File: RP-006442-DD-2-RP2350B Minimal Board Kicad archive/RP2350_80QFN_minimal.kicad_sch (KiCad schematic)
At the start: 51 parts, among them J1 USB_C_Receptacle_USB2.0_16P, J2 Conn_02x26_Odd_Even, J3 Conn_02x26_Odd_Even, J4 SM03B-SRSS-TB, SW1 SW_Push, SW2 SW_Push, U1 RP2350_80QFN, U2 NCP1117-3.3_SOT223, U3 W25Q128JVS, U4 DNF, Y1 ABM8-272-T3

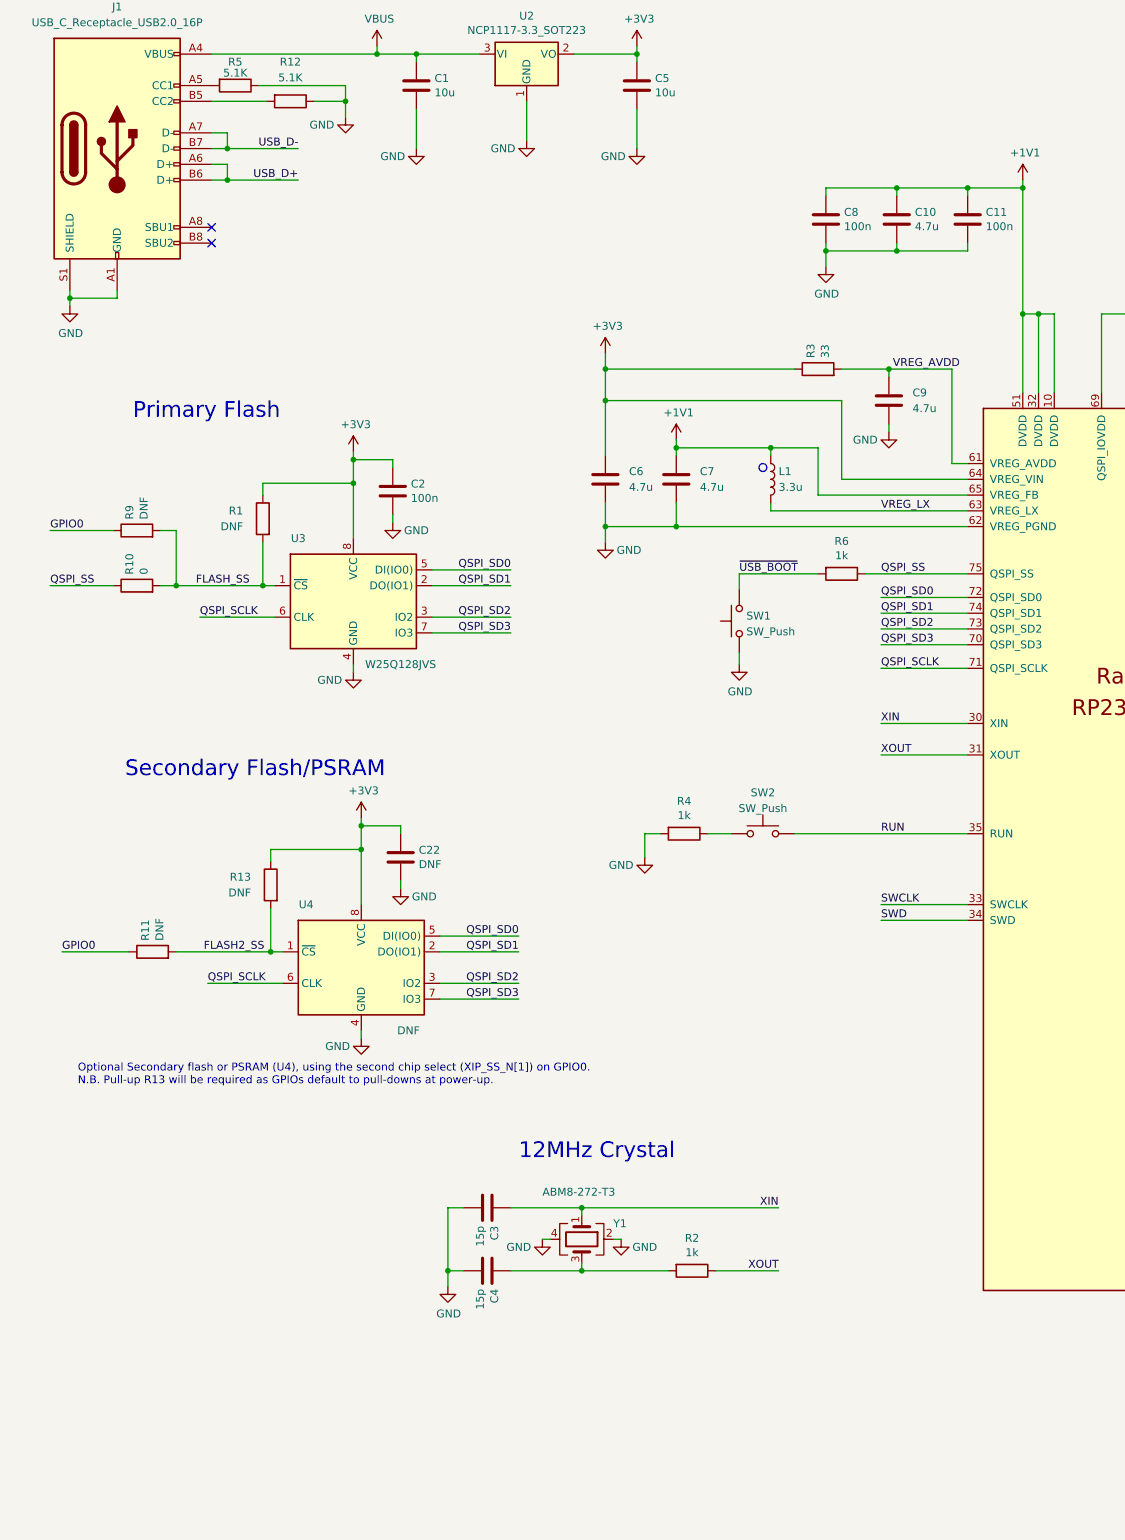
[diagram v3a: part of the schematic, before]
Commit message: added leds schematic page
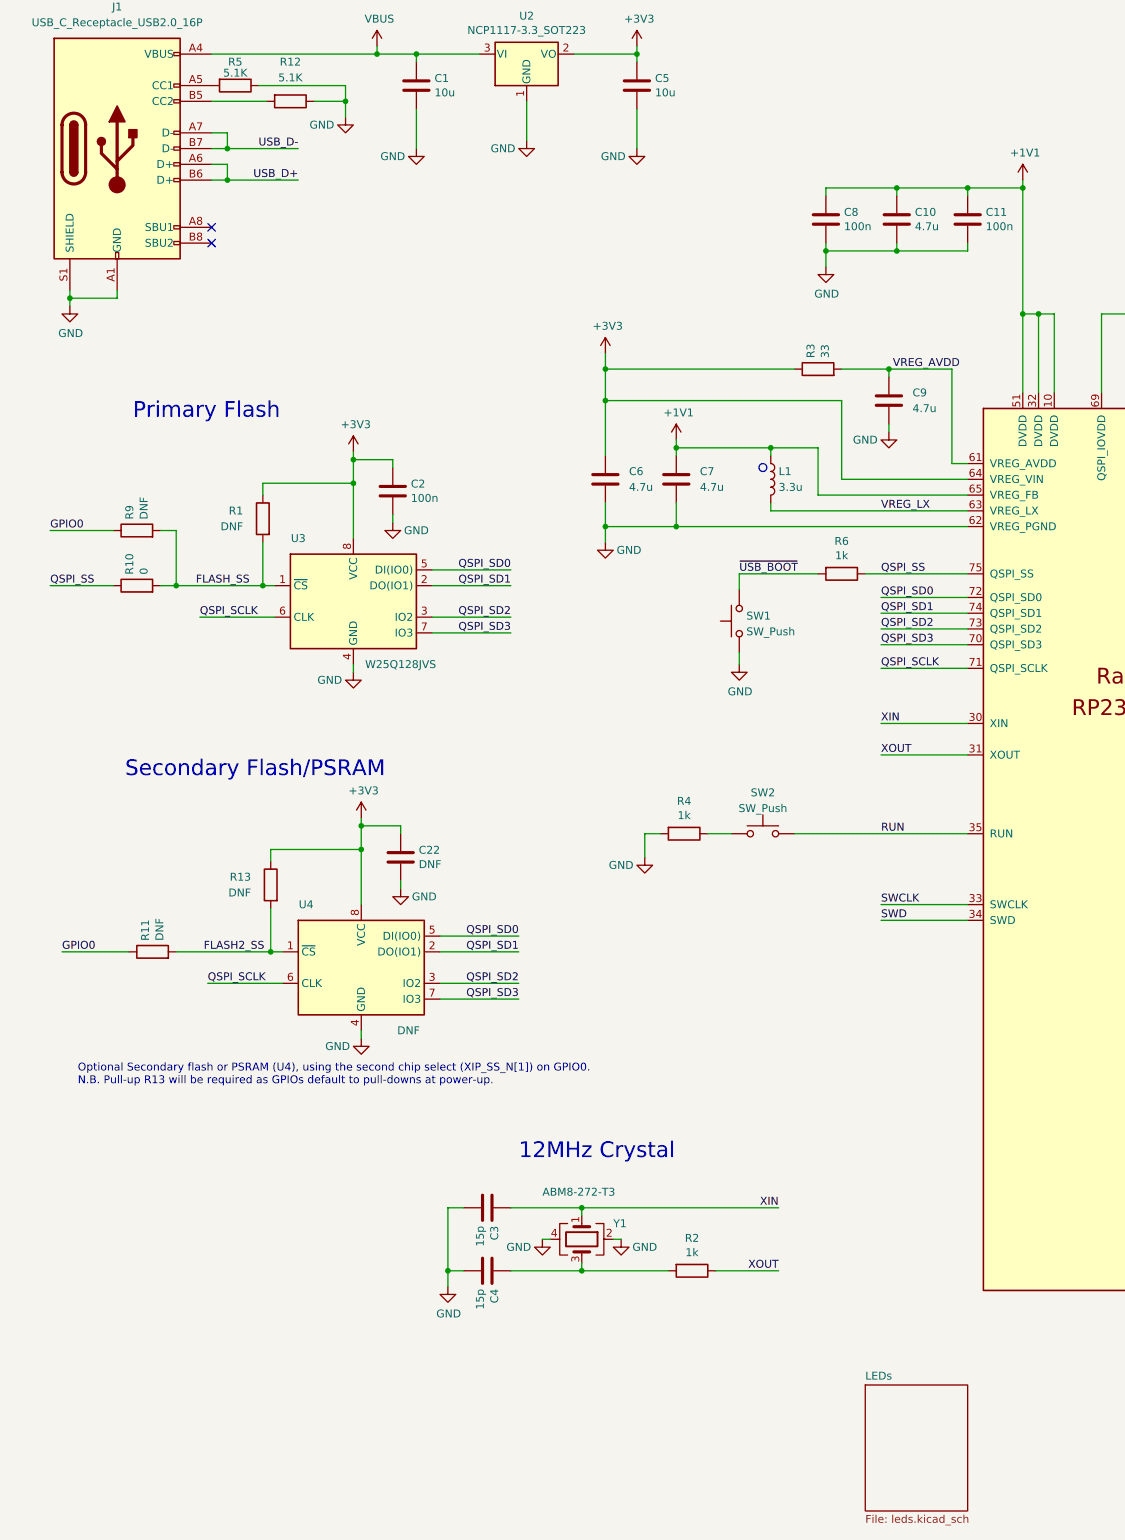
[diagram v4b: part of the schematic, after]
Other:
- added sheet LEDs (leds.kicad_sch)
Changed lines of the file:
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@@
 (kicad_sch
-	(version 20231120)
+	(version 20250114)
 	(generator "eeschema")
-	(generator_version "8.0")
+	(generator_version "9.0")
 	(paper "A3")
 	(title_block
@@
 		(company "Raspberry Pi Ltd")
 	)
+	(circle
+		(center 133.35 106.045)
+		(radius 0.635)
+		(stroke
+			(width 0)
+			(type default)
+			(color 132 0 0 1)
+		)
+		(fill
+			(type color)
+			(color 132 0 0 1)
+		)
+	)
+	(text "Optional Secondary flash or PSRAM (U4), using the second chip select (XIP_SS_N[1]) on GPIO0.\nN.B. Pull-up R13 will be required as GPIOs default to pull-downs at power-up."
+		(exclude_from_sim no)
+		(at 22.86 205.74 0)
+		(effects
+			(font
+				(size 1.27 1.27)
+			)
+			(justify left bottom)
+		)
+	)
+	(text "IOs"
+		(exclude_from_sim no)
+		(at 360.68 109.22 0)
+		(effects
+			(font
+				(size 2.54 2.54)
+			)
+			(justify left bottom)
+		)
+	)
+	(text "12MHz Crystal"
+		(exclude_from_sim no)
+		(at 93.98 217.805 0)
+		(effects
+			(font
+				(size 2.54 2.54)
+			)
+			(justify left bottom)
+		)
+	)
+	(text "Primary Flash"
+		(exclude_from_sim no)
+		(at 31.75 98.425 0)
+		(effects
+			(font
+				(size 2.54 2.54)
+			)
+			(justify left bottom)
+		)
+	)
+	(text "JST Debug Connector"
+		(exclude_from_sim no)
+		(at 328.93 210.82 0)
+		(effects
+			(font
+				(size 1.27 1.27)
+			)
+			(justify left bottom)
+		)
+	)
+	(text "Make sure R7 and R8 are close to RP2350\n"
+		(exclude_from_sim no)
+		(at 252.73 100.33 0)
+		(effects
+			(font
+				(size 1.27 1.27)
+			)
+			(justify left bottom)
+		)
+	)
+	(text "Secondary Flash/PSRAM"
+		(exclude_from_sim no)
+		(at 30.48 156.21 0)
+		(effects
+			(font
+				(size 2.54 2.54)
+			)
+			(justify left bottom)
+		)
+	)
+	(text "Power"
+		(exclude_from_sim no)
+		(at 73.66 27.94 0)
+		(effects
+			(font
+				(size 2.54 2.54)
+			)
+			(justify left bottom)
+		)
+	)
 	(junction
 		(at 119.38 115.57)
@@
 		)
 	)
-	(circle
-		(center 133.35 106.045)
-		(radius 0.635)
-		(stroke
-			(width 0)
-			(type default)
-			(color 132 0 0 1)
-		)
-		(fill
-			(type color)
-			(color 132 0 0 1)
-		)
-	)
-	(text "Optional Secondary flash or PSRAM (U4), using the second chip select (XIP_SS_N[1]) on GPIO0.\nN.B. Pull-up R13 will be required as GPIOs default to pull-downs at power-up."
-		(exclude_from_sim no)
-		(at 22.86 205.74 0)
-		(effects
-			(font
-				(size 1.27 1.27)
-			)
-			(justify left bottom)
-		)
-	)
-	(text "IOs"
-		(exclude_from_sim no)
-		(at 360.68 109.22 0)
-		(effects
-			(font
-				(size 2.54 2.54)
-			)
-			(justify left bottom)
-		)
-	)
-	(text "12MHz Crystal"
-		(exclude_from_sim no)
-		(at 93.98 217.805 0)
-		(effects
-			(font
-				(size 2.54 2.54)
-			)
-			(justify left bottom)
-		)
-	)
-	(text "Primary Flash"
-		(exclude_from_sim no)
-		(at 31.75 98.425 0)
-		(effects
-			(font
-				(size 2.54 2.54)
-			)
-			(justify left bottom)
-		)
-	)
-	(text "JST Debug Connector"
-		(exclude_from_sim no)
-		(at 328.93 210.82 0)
-		(effects
-			(font
-				(size 1.27 1.27)
-			)
-			(justify left bottom)
-		)
-	)
-	(text "Make sure R7 and R8 are close to RP2350\n"
-		(exclude_from_sim no)
-		(at 252.73 100.33 0)
-		(effects
-			(font
-				(size 1.27 1.27)
-			)
-			(justify left bottom)
-		)
-	)
-	(text "Secondary Flash/PSRAM"
-		(exclude_from_sim no)
-		(at 30.48 156.21 0)
-		(effects
-			(font
-				(size 2.54 2.54)
-			)
-			(justify left bottom)
-		)
-	)
-	(text "Power"
-		(exclude_from_sim no)
-		(at 73.66 27.94 0)
-		(effects
-			(font
-				(size 2.54 2.54)
-			)
-			(justify left bottom)
-		)
-	)
 	(label "XIN"
 		(at 152.4 147.32 0)
@@
 		(at 271.78 227.33)
 		(size 20.32 17.78)
+		(exclude_from_sim no)
+		(in_bom yes)
+		(on_board yes)
+		(dnp no)
 		(fields_autoplaced yes)
 		(stroke
@@
 		(at 273.05 193.04)
 		(size 25.4 20.32)
+		(exclude_from_sim no)
+		(in_bom yes)
+		(on_board yes)
+		(dnp no)
 		(fields_autoplaced yes)
 		(stroke
@@
 		(at 271.78 157.48)
 		(size 20.32 16.51)
+		(exclude_from_sim no)
+		(in_bom yes)
+		(on_board yes)
+		(dnp no)
 		(fields_autoplaced yes)
 		(stroke
@@
 		)
 	)
+	(sheet
+		(at 149.86 254)
+		(size 16.51 20.32)
+		(exclude_from_sim no)
+		(in_bom yes)
+		(on_board yes)
+		(dnp no)
+		(fields_autoplaced yes)
+		(stroke
+			(width 0.1524)
+			(type solid)
+		)
+		(fill
+			(color 0 0 0 0.0000)
+		)
+		(property "Sheetname" "LEDs"
+			(at 149.86 253.2884 0)
+			(effects
+				(font
+					(size 1.27 1.27)
+				)
+				(justify left bottom)
+			)
+		)
+		(property "Sheetfile" "leds.kicad_sch"
+			(at 149.86 274.9046 0)
+			(effects
+				(font
+					(size 1.27 1.27)
+				)
+				(justify left top)
+			)
+		)
+		(instances
+			(project "RP2350_80QFN_minimal"
+				(path "/94683f5c-9cd9-448e-be96-9792537b5cb8"
+					(page "5")
+				)
+			)
+		)
+	)
 	(sheet_instances
 		(path "/"
@@
 		)
 	)
+	(embedded_fonts no)
 )

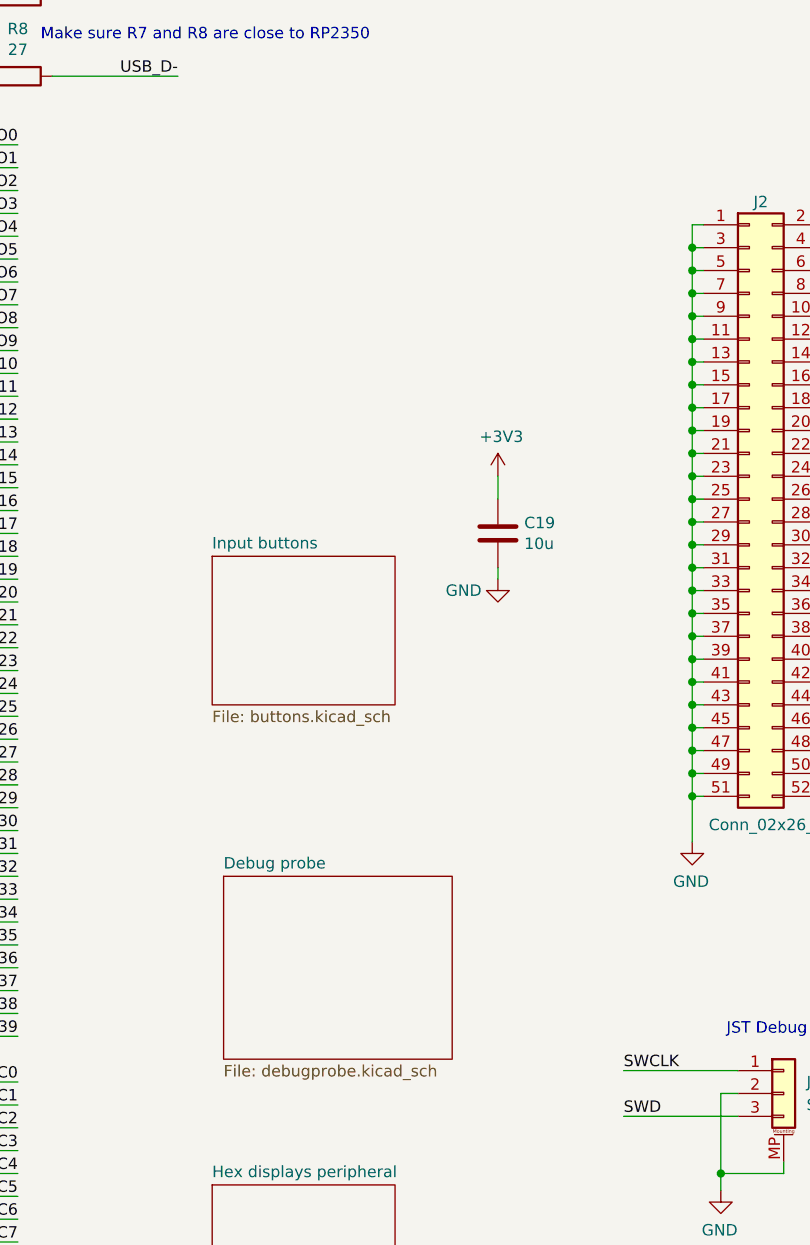
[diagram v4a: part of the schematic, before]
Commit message: Placed hierarchical labels in debugprobe
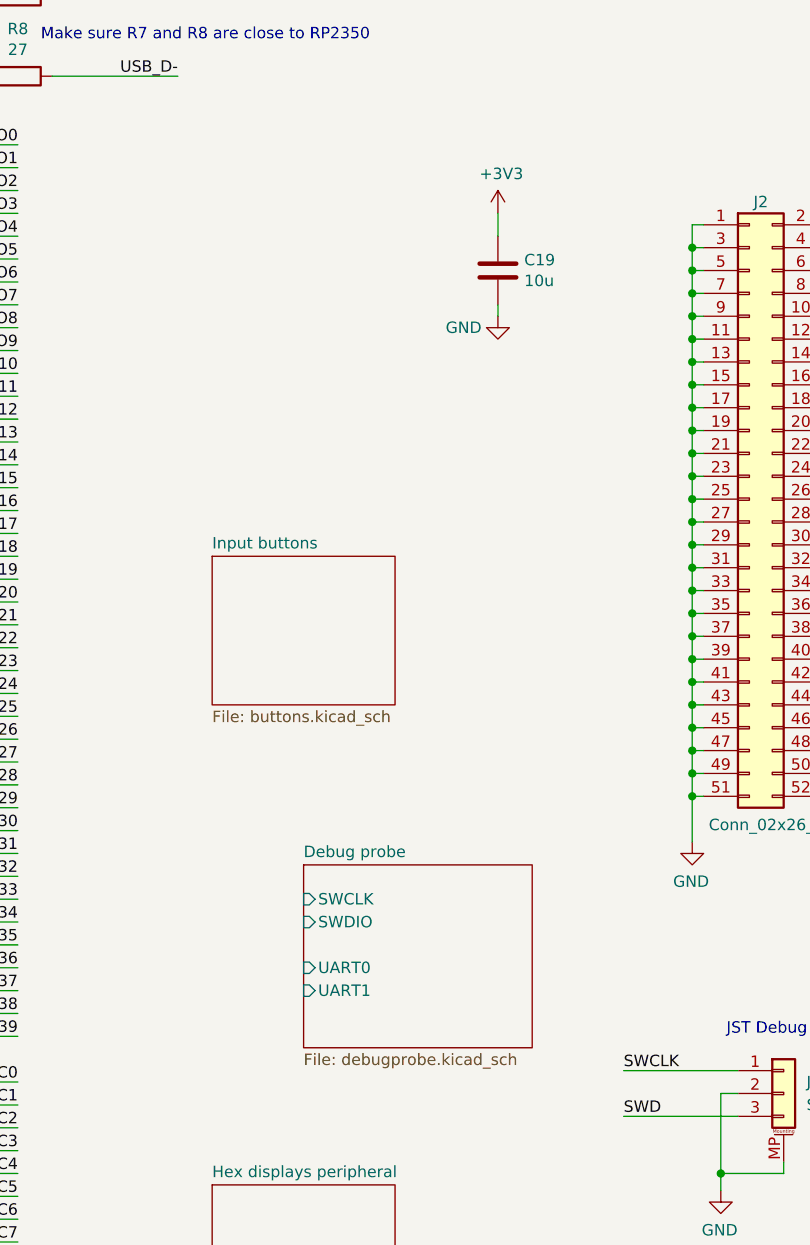
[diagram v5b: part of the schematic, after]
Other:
- sheet Debug probe ports: added SWCLK, SWDIO, UART0, UART1; removed none
- moved on the sheet: C19
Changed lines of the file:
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@@
 	(wire
 		(pts
-			(xy 303.53 148.59) (xy 303.53 151.13)
+			(xy 303.53 119.38) (xy 303.53 121.92)
 		)
 		(stroke
@@
 	(wire
 		(pts
-			(xy 303.53 158.75) (xy 303.53 160.02)
+			(xy 303.53 129.54) (xy 303.53 130.81)
 		)
 		(stroke
@@
 	(symbol
 		(lib_id "power:+3V3")
-		(at 303.53 148.59 0)
+		(at 303.53 119.38 0)
 		(unit 1)
 		(exclude_from_sim no)
@@
 		(dnp no)
 		(property "Reference" "#PWR023"
-			(at 303.53 152.4 0)
+			(at 303.53 123.19 0)
 			(effects
 				(font
@@
 		)
 		(property "Value" "+3V3"
-			(at 303.911 144.1958 0)
+			(at 303.911 114.9858 0)
 			(effects
 				(font
@@
 		)
 		(property "Footprint" ""
-			(at 303.53 148.59 0)
+			(at 303.53 119.38 0)
 			(effects
 				(font
@@
 		)
 		(property "Datasheet" ""
-			(at 303.53 148.59 0)
+			(at 303.53 119.38 0)
 			(effects
 				(font
@@
 		)
 		(property "Description" ""
-			(at 303.53 148.59 0)
+			(at 303.53 119.38 0)
 			(effects
 				(font
@@
 	(symbol
 		(lib_id "Device:C")
-		(at 303.53 154.94 0)
+		(at 303.53 125.73 0)
 		(unit 1)
 		(exclude_from_sim no)
@@
 		(dnp no)
 		(property "Reference" "C19"
-			(at 306.451 153.7716 0)
+			(at 306.451 124.5616 0)
 			(effects
 				(font
@@
 		)
 		(property "Value" "10u"
-			(at 306.451 156.083 0)
+			(at 306.451 126.873 0)
 			(effects
 				(font
@@
 		)
 		(property "Footprint" "Capacitor_SMD:C_0805_2012Metric"
-			(at 304.4952 158.75 0)
+			(at 304.4952 129.54 0)
 			(effects
 				(font
@@
 		)
 		(property "Datasheet" "~"
-			(at 303.53 154.94 0)
+			(at 303.53 125.73 0)
 			(effects
 				(font
@@
 		)
 		(property "Description" ""
-			(at 303.53 154.94 0)
+			(at 303.53 125.73 0)
 			(effects
 				(font
@@
 	(symbol
 		(lib_id "power:GND")
-		(at 303.53 160.02 0)
+		(at 303.53 130.81 0)
 		(unit 1)
 		(exclude_from_sim no)
@@
 		(dnp no)
 		(property "Reference" "#PWR024"
-			(at 303.53 166.37 0)
+			(at 303.53 137.16 0)
 			(effects
 				(font
@@
 		)
 		(property "Value" "GND"
-			(at 299.72 161.29 0)
+			(at 299.72 132.08 0)
 			(effects
 				(font
@@
 		)
 		(property "Footprint" ""
-			(at 303.53 160.02 0)
+			(at 303.53 130.81 0)
 			(effects
 				(font
@@
 		)
 		(property "Datasheet" ""
-			(at 303.53 160.02 0)
+			(at 303.53 130.81 0)
 			(effects
 				(font
@@
 		)
 		(property "Description" ""
-			(at 303.53 160.02 0)
+			(at 303.53 130.81 0)
 			(effects
 				(font
@@
 	)
 	(sheet
-		(at 273.05 193.04)
+		(at 281.94 191.77)
 		(size 25.4 20.32)
 		(exclude_from_sim no)
@@
 		)
 		(property "Sheetname" "Debug probe"
-			(at 273.05 192.3284 0)
+			(at 281.94 191.0584 0)
 			(effects
 				(font
@@
 		)
 		(property "Sheetfile" "debugprobe.kicad_sch"
-			(at 273.05 213.9446 0)
+			(at 281.94 212.6746 0)
 			(effects
 				(font
@@
 			)
 		)
+		(pin "SWCLK" input
+			(at 281.94 195.58 180)
+			(effects
+				(font
+					(size 1.27 1.27)
+				)
+				(justify left)
+			)
+		)
+		(pin "SWDIO" input
+			(at 281.94 198.12 180)
+			(effects
+				(font
+					(size 1.27 1.27)
+				)
+				(justify left)
+			)
+		)
+		(pin "UART0" input
+			(at 281.94 203.2 180)
+			(effects
+				(font
+					(size 1.27 1.27)
+				)
+				(justify left)
+			)
+		)
+		(pin "UART1" input
+			(at 281.94 205.74 180)
+			(effects
+				(font
+					(size 1.27 1.27)
+				)
+				(justify left)
+			)
+		)
